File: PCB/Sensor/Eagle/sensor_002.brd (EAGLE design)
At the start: 142.8 x 97.5 mm, 254 parts, among them IC1 LMV324, IC10 LMV324, IC11 LMV324, IC12 LMV324, IC13 LMV324, IC14 LMV324, IC15 LMV324, IC16 LMV324, IC17 LMV324, IC18 LMV324, IC19 LMV324, IC2 LMV324, IC20 LMV324, IC21 LMV324, IC22 LMV324, IC23 LMV324, IC24 LMV324, IC3 LMV324, IC4 LMV324, IC5 LMV324, IC6 LMV324, IC7 LMV324, IC8 LMV324, IC9 LMV324, U1 74HC4067, U2 74HC4067, U3 74HC4067, U4 74HC4067, U5 74HC4067, U6 74HC4067, X1 MKDSN1,5/2-5,08, X2 MKDSN1,5/10-5,08

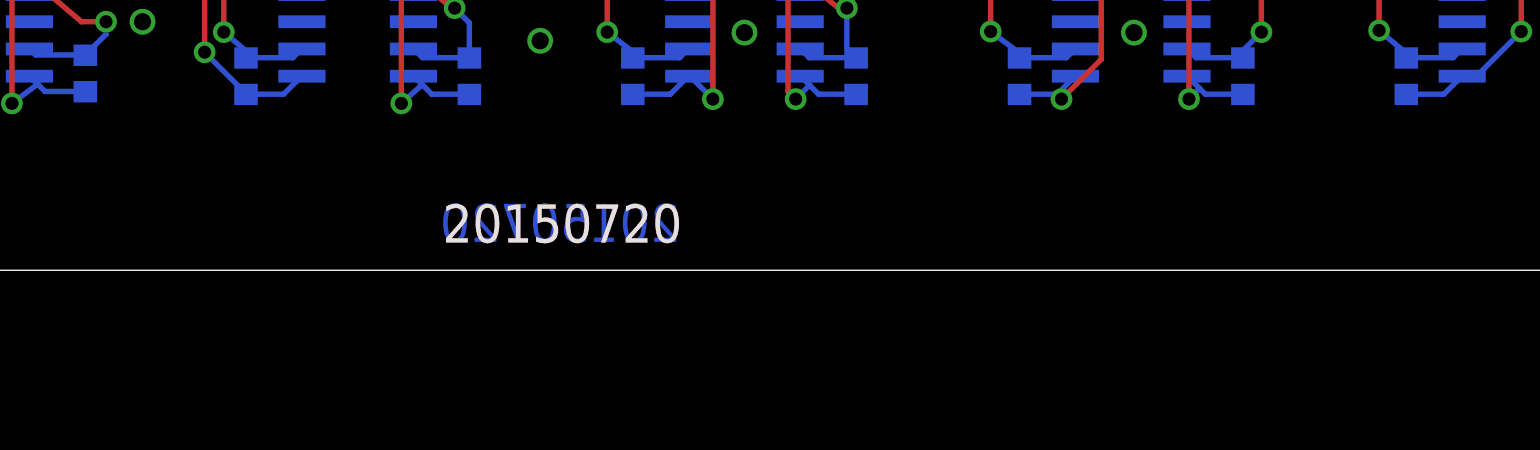
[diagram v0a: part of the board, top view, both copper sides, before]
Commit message: PCB modification, CERN license
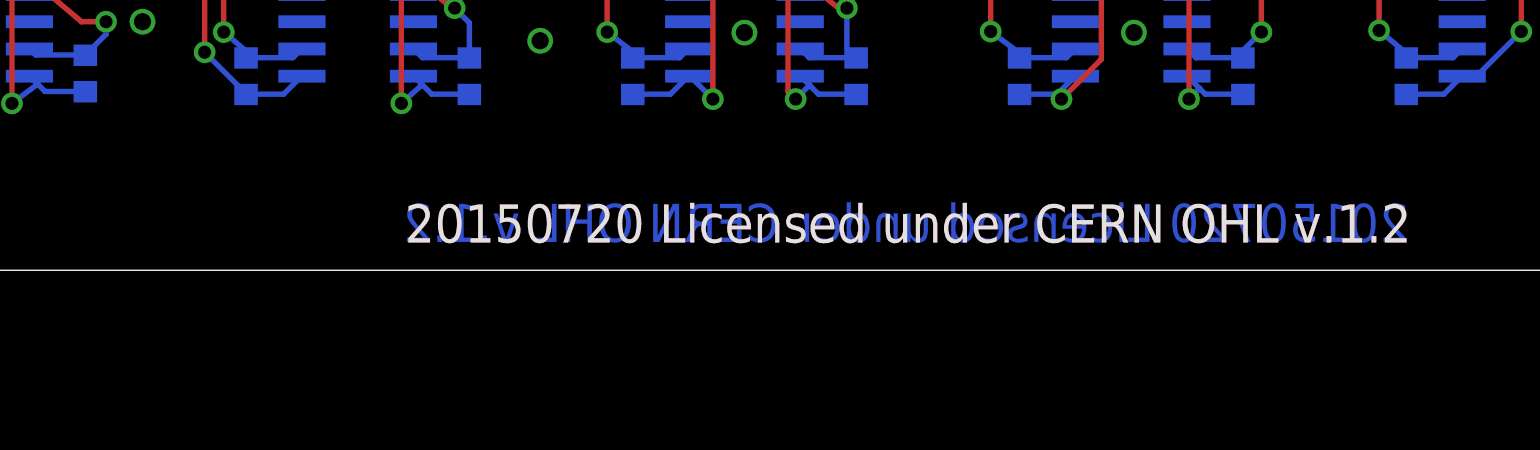
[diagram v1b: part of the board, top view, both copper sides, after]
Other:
- board text added: "20150720 Licensed under CERN OHL v.1.2"
- board text removed: "20150720"
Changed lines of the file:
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@@
 <rectangle x1="58.3572" y1="78.6462" x2="61.9132" y2="111.6662" layer="41" rot="R90"/>
 <rectangle x1="58.3572" y1="78.6462" x2="61.9132" y2="111.6662" layer="42" rot="R90"/>
-<text x="56.9588" y="3.0696" size="1.778" layer="1" font="vector" ratio="15" rot="R180">20150720</text>
-<text x="56.8388" y="1.3196" size="1.778" layer="16" font="vector" ratio="15" rot="MR0">20150720</text>
-<rectangle x1="50.9272" y1="-14.1838" x2="54.4832" y2="18.8362" layer="41" rot="R90"/>
-<rectangle x1="50.9272" y1="-14.1838" x2="54.4832" y2="18.8362" layer="42" rot="R90"/>
+<text x="90.9588" y="3.0696" size="1.778" layer="1" font="vector" ratio="15" rot="R180">20150720 Licensed under CERN OHL v.1.2</text>
+<text x="90.8388" y="1.3196" size="1.778" layer="16" font="vector" ratio="15" rot="MR0">20150720 Licensed under CERN OHL v.1.2</text>
 <wire x1="0" y1="5" x2="0" y2="92.48" width="0.02" layer="20"/>
 <wire x1="0" y1="92.48" x2="5" y2="97.48" width="0.02" layer="20" curve="-90"/>
@@
 <text x="62.9188" y="96.1996" size="1.778" layer="25" font="vector" ratio="15" rot="R180">Miriam</text>
 <text x="62.4688" y="94.4396" size="1.778" layer="26" font="vector" ratio="15" rot="MR0">Miriam</text>
-<text x="56.8388" y="1.3196" size="1.778" layer="26" font="vector" ratio="15" rot="MR0">20150720</text>
-<text x="56.9588" y="3.0696" size="1.778" layer="25" font="vector" ratio="15" rot="R180">20150720</text>
+<text x="90.8388" y="1.3196" size="1.778" layer="26" font="vector" ratio="15" rot="MR0">20150720 Licensed under CERN OHL v.1.2</text>
+<text x="90.9588" y="3.0696" size="1.778" layer="25" font="vector" ratio="15" rot="R180">20150720 Licensed under CERN OHL v.1.2</text>
+<rectangle x1="30" y1="1" x2="92" y2="4" layer="41"/>
+<rectangle x1="30" y1="1" x2="92" y2="4" layer="42"/>
 </plain>
 <attributes>
